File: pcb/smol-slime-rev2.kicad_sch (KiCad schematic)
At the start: 23 parts, among them J1 BATTERY, SW1 TS-1088-AR02016, U1 nPM1300, U2 LSM6DSV16X, U3 QMC6309

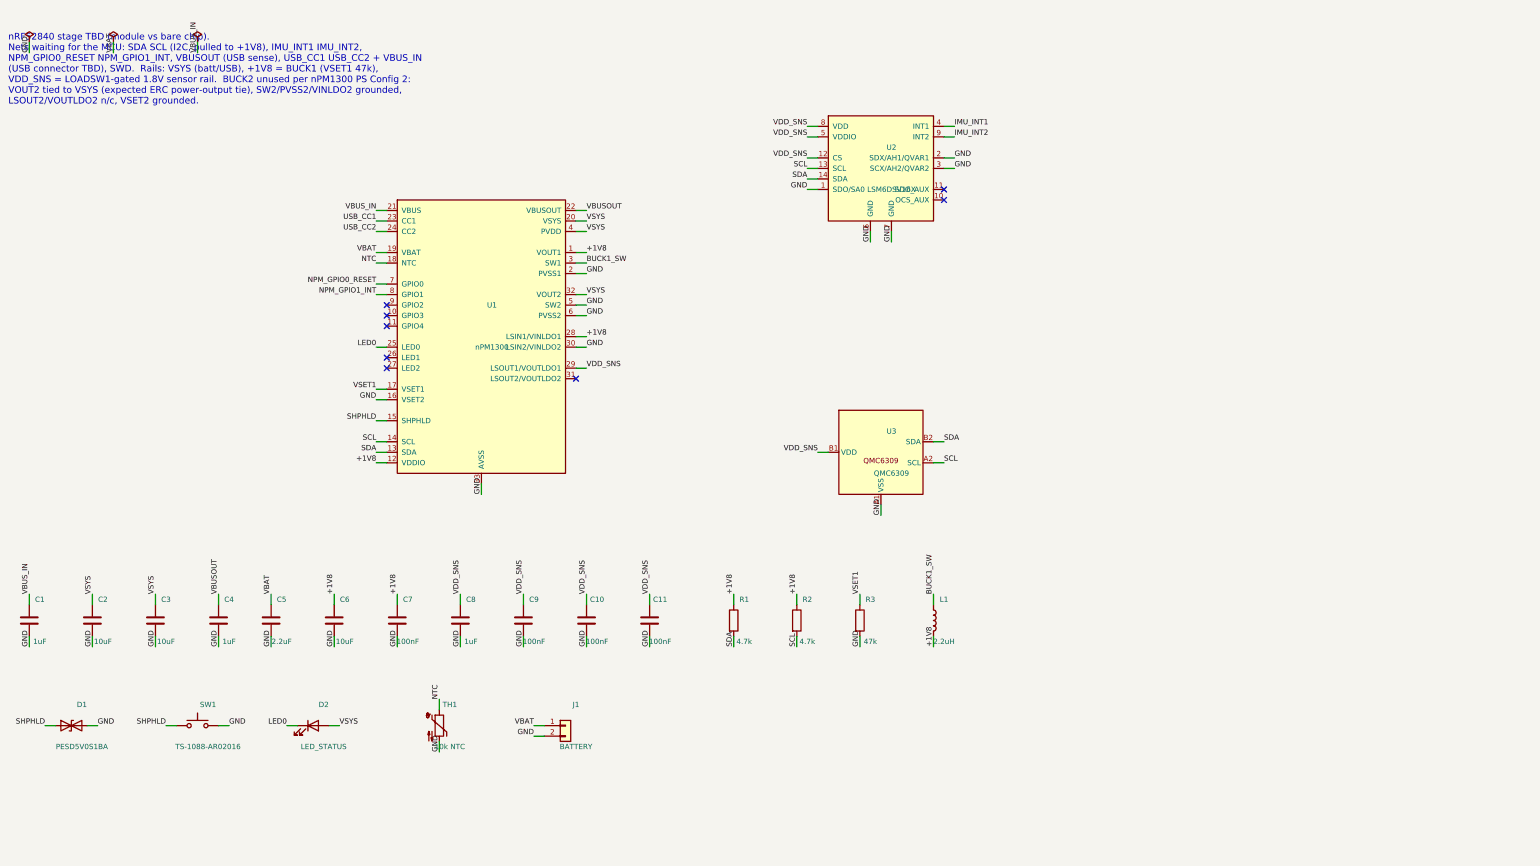
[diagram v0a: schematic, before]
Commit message: Wire the nRF52840 stage as a bare chip with custom antenna feed
The module route died on a supply reality: no JLCPCB-stocked nRF52840
module exposes its RF path for a custom on-PCB antenna. The Ebyte
E73-S1C keeps its ceramic antenna on the module, the S1CX only offers
an IPEX connector, and nothing from Raytac, Minew, or Holyiot is
stocked at all. The bare nRF52840-QIAA is meanwhile a Basic part with
over a thousand units, so rev 2 uses the bare chip and owns the
antenna.

The schematic now follows the nRF52840 Product Spec v1.11 section
7.3.5 circuit configuration 5: VDD and VDDH on the 1.8 V rail from the
nPM1300, REG1 DC/DC with the 15 nH plus 10 uH filter chain, the full
DEC decoupling set, a 32 MHz crystal with 12 pF loads, USB data lines
to labels pending a connector, and the reference RF match feeding an
RF_ANT net for the printed antenna. SWD and VTref/reset programming
pads use the existing PinPads footprints. The 32.768 kHz crystal is
omitted in favour of the LFRC, and NFC is unused. ERC findings are
down to the expected set enumerated in the sheet note.
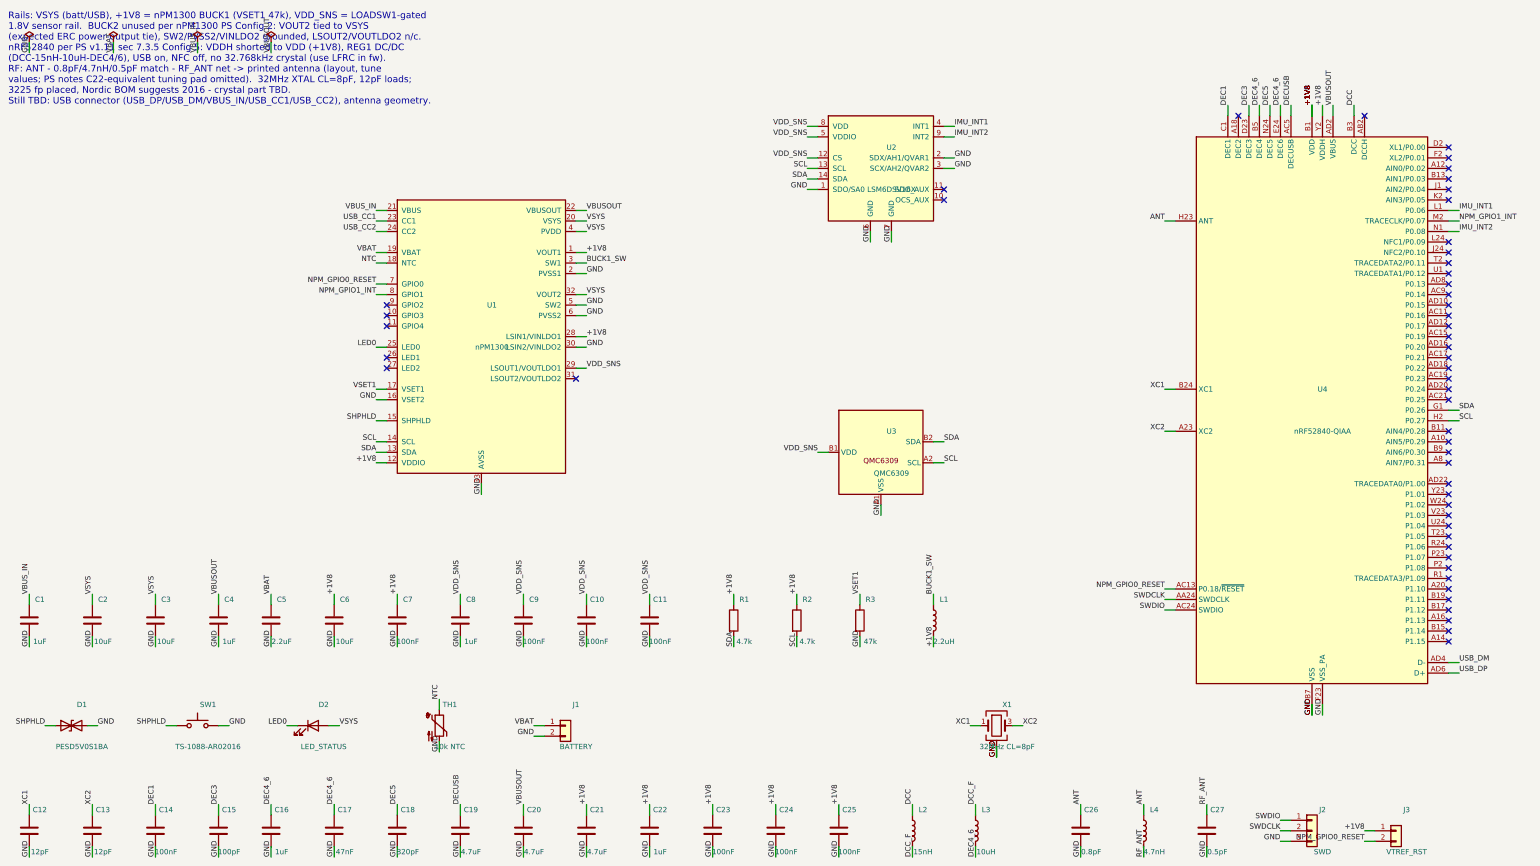
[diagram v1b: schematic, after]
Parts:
- added C12, C13: 12pF, Capacitor_SMD:C_0603_1608Metric, symbol Device:C
- added C14, C23, C24, C25: 100nF, Capacitor_SMD:C_0603_1608Metric, symbol Device:C
- added C15: 100pF, Capacitor_SMD:C_0603_1608Metric, symbol Device:C
- added C16, C22: 1uF, Capacitor_SMD:C_0603_1608Metric, symbol Device:C
- added C17: 47nF, Capacitor_SMD:C_0603_1608Metric, symbol Device:C
- added C18: 820pF, Capacitor_SMD:C_0603_1608Metric, symbol Device:C
- added C19, C20, C21: 4.7uF, Capacitor_SMD:C_0603_1608Metric, symbol Device:C
- added C26: 0.8pF, Capacitor_SMD:C_0402_1005Metric, symbol Device:C
- added C27: 0.5pF, Capacitor_SMD:C_0402_1005Metric, symbol Device:C
- added J2: SWD, smol-biscuits:PinPads_1x03_P2.54mm, symbol Connector_Generic:Conn_01x03
- added J3: VTREF_RST, smol-biscuits:PinPads_1x02_P2.54mm, symbol Connector_Generic:Conn_01x02
- added L2: 15nH, Inductor_SMD:L_0402_1005Metric, symbol Device:L
- added L3: 10uH, Inductor_SMD:L_0603_1608Metric, symbol Device:L
- added L4: 4.7nH, Inductor_SMD:L_0402_1005Metric, symbol Device:L
- added U4: nRF52840-QIAA, Package_DFN_QFN:Nordic_AQFN-73-1EP_7x7mm_P0.5mm, symbol MCU_Nordic:nRF52840
- added X1: 32MHz CL=8pF, smol-biscuits:Crystal_SMD_3225-4Pin_3.2x2.5mm_Silkscreenfix, symbol Device:Crystal_GND24
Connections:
- net +1V8: now also C21.1, C22.1, C23.1, C24.1, C25.1, J3.1 (Pin_1), U4.A22 (VDD), U4.AD14 (VDD), U4.AD23 (VDD), U4.B1 (VDD), U4.W1 (VDD), U4.Y2 (VDDH)
- net GND: now also C12.2, C13.2, C14.2, C15.2, C16.2, C17.2, C18.2, C19.2, C20.2, C21.2, C22.2, C23.2, C24.2, C25.2, C26.2, C27.2, J2.3 (Pin_3), U4.B7 (VSS), U4.EP (VSS), U4.F23 (VSS_PA), X1.2 (G), X1.4 (G)
- net IMU_INT1: now also U4.L1 (P0.06)
- net IMU_INT2: now also U4.N1 (P0.08)
- net NPM_GPIO0_RESET: now also J3.2 (Pin_2), U4.AC13 (P0.18/~{RESET})
- net NPM_GPIO1_INT: now also U4.M2 (TRACECLK/P0.07)
- net SCL: now also U4.H2 (P0.27)
- net SDA: now also U4.G1 (P0.26)
- net VBUSOUT: now also C20.1, U4.AD2 (VBUS)
- new net ANT: C26.1, L4.1, U4.H23 (ANT)
- new net DCC: L2.1, U4.B3 (DCC)
- new net DCC_F: L2.2, L3.1
- new net DEC1: C14.1, U4.C1 (DEC1)
- new net DEC3: C15.1, U4.D23 (DEC3)
- new net DEC4_6: C16.1, C17.1, L3.2, U4.B5 (DEC4), U4.E24 (DEC6)
- new net DEC5: C18.1, U4.N24 (DEC5)
- new net DECUSB: C19.1, U4.AC5 (DECUSB)
- new net RF_ANT: C27.1, L4.2
- new net SWDCLK: J2.2 (Pin_2), U4.AA24 (SWDCLK)
- new net SWDIO: J2.1 (Pin_1), U4.AC24 (SWDIO)
- new net USB_DM: U4.AD4 (D-)
- new net USB_DP: U4.AD6 (D+)
- new net XC1: C12.1, U4.B24 (XC1), X1.1
- new net XC2: C13.1, U4.A23 (XC2), X1.3
- no-connect marks 8 -> 52
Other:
- note added: "Rails: VSYS (batt/USB), +1V8 = nPM1300 BUCK1 (VSET1 47k), VDD_SNS = LOADSW1-gated 1.8V sensor rail. BUCK2 unused per nPM1300 PS Config 2: VOUT2 tied to VSYS (expected ERC power-output tie), SW2/PVSS2/VINLDO2 grounded, LSOUT2/VOUTLDO2 n/c. nRF52840 per PS v1.11 sec 7.3.5 Config 5: VDDH shorted to VDD (+1V8), REG1 DC/DC (DCC-15nH-10uH-DEC4/6), USB on, NFC off, no 32.768kHz crystal (use LFRC in fw).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"
- note removed: "nRF52840 stage TBD (module vs bare chip). Nets waiting for the MCU: SDA SCL (I2C, pulled to +1V8), IMU_INT1 IMU_INT2, NPM_GPIO0_RESET NPM_GPIO1_INT, VBUSOUT (USB sense), USB_CC1 USB_CC2 + VBUS_IN (USB connector TBD), SWD. Rails: VSYS (batt/USB), +1V8 = BUCK1 (VSET1 47k), VDD_SNS = LOADSW1-gated 1.8V sensor rail. BUCK2 unused per nPM1300 PS Config 2: VOUT2 tied to VSYS (expected ERC power-output t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"

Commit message: Add antenna tuning pad, part datasheets, and rev 2 handoff notes
The antenna is fully custom etched copper, so the schematic now carries
a DNP 0402 shunt pad at the RF_ANT feed for match tuning, mirroring the
N.C. provision in Nordic's reference circuit. Purchasing is no longer
assumed to go through JLCPCB assembly; parts may come from Digikey or
Mouser and be hand-soldered, which puts genuine manufacturers back on
the table for the TVS and friends.

docs/ gains the full datasheets for every rev 2 part: nRF52840 PS
v1.11, nPM1300 PS v1.1, LSM6DSV16X DS13510, the TS-1088 switch, and
the PESD5V0S1BA TVS. rev2-todo.md writes up the remaining work on
Sandra's side: antenna design and tuning, symbol and footprint reviews,
a distributor-friendly shopping list, the USB connector decision,
layout and hand-assembly notes, and the firmware task list.
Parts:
- added C28: DNP, Capacitor_SMD:C_0402_1005Metric, symbol Device:C
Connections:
- net GND: now also C28.2
- net RF_ANT: now also C28.1

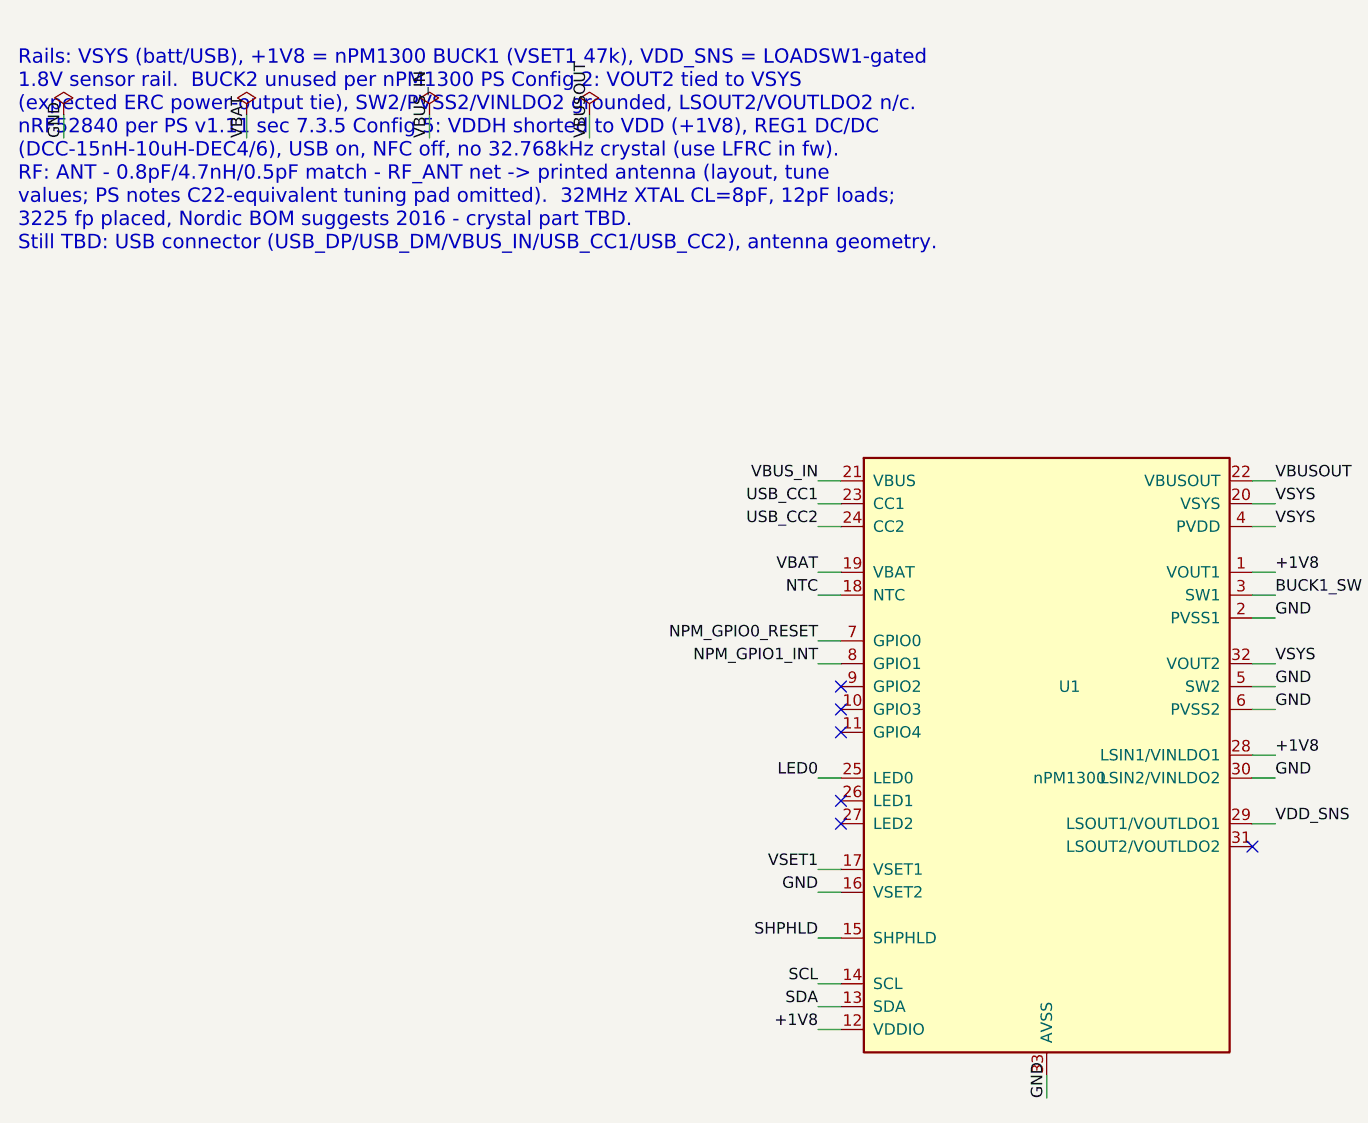
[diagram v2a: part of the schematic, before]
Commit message: Wire mid-mount USB-C connector
J4 is the Korean Hroparts TYPE-C-31-M-17, a mid-mount sink-type 16-pin
USB 2.0 receptacle at about nine cents, picked for the low-profile
wearable stack: the board gets a cutout and the connector hangs in it,
roughly halving the height. KiCad ships the footprint including the
cutout outline. VBUS, D+/D-, and the CC lines all land on the nPM1300
side nets; CC detection is inside the PMIC so the board carries no CC
resistors, SBU is no-connect, and the shell is grounded.

With the connector in, ERC is down to the four deliberate straps noted
on the sheet: the Nordic VOUT2 to VSYS tie, the VBUSOUT power flag,
and the IMU address and aux-disable grounds. The schematic has no
undriven or dangling nets left. Datasheet added to docs.
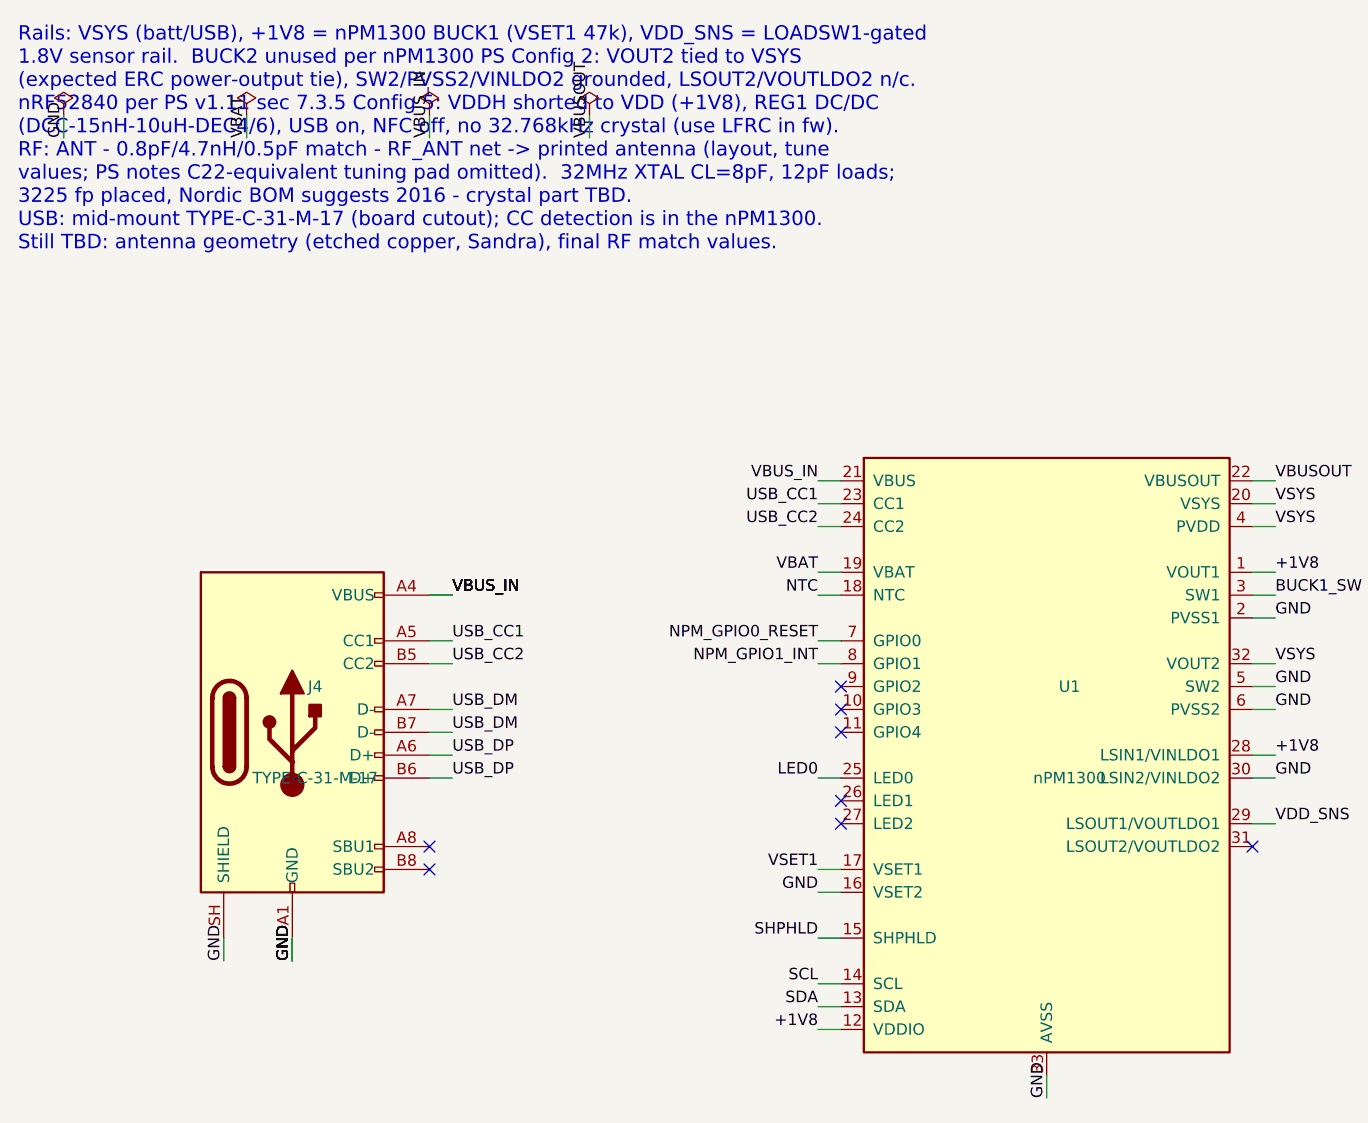
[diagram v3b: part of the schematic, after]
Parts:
- added J4: TYPE-C-31-M-17, Connector_USB:USB_C_Receptacle_HRO_TYPE-C-31-M-17, symbol Connector:USB_C_Receptacle_USB2.0_16P
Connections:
- net GND: now also J4.A1 (GND), J4.A12 (GND), J4.B1 (GND), J4.B12 (GND), J4.SH (SHIELD)
- net USB_CC1: now also J4.A5 (CC1)
- net USB_CC2: now also J4.B5 (CC2)
- net USB_DM: now also J4.A7 (D-), J4.B7 (D-)
- net USB_DP: now also J4.A6 (D+), J4.B6 (D+)
- net VBUS_IN: now also J4.A4 (VBUS), J4.A9 (VBUS), J4.B4 (VBUS), J4.B9 (VBUS)
- no-connect marks 52 -> 54

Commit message: Redraw rev 2 schematic with wired clusters and grouped placement
The first draft was pure stub-and-label netlist style, which is
electrically complete but reads as scattered parts. The sheet now draws
real wires for the circuits where shape carries meaning: the SHPHLD
button rail with the switch and TVS hanging in parallel, the BUCK1
switch node through the 2.2 uH inductor, and the RF chain from the ANT
ball through the 0.8 pF / 4.7 nH / 0.5 pF match and DNP tuning pad to
the RF_ANT feed. Decoupling and power distribution stay label-based as
usual, but every group now sits with its owner: crystal and load caps
by the XC pins, DEC caps under the nRF, sensor-rail caps by the IMU,
and the SWD pads beside the MCU. IC reference and value text moved
outside the symbol bodies.

Nothing electrical changed: the exported netlist is identical to the
previous commit across all 35 nets, and ERC still reports exactly the
four deliberate straps.
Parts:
- C12, C13: footprint Capacitor_SMD:C_0603_1608Metric -> Capacitor_SMD:C_0402_1005Metric

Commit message: Size passives per the Nordic reference BOMs
0603 everywhere was a hand-solder-friendly simplification inherited
from rev 1. The reference designs are one size finer for the small
values, and on a wearable the area matters, so the schematic now
matches them: sub-microfarad capacitors (100nF, 820pF, 100pF, 47nF,
12pF) and the three resistors move to 0402, joining the RF parts that
were already there. Bulk capacitors of a microfarad and up stay 0603
for DC-bias derating, and the NTC stays 0603 to suit the common 10k
thermistor parts. Net result: 21 passives at 0402, 15 at 0603.

Netlist verified identical; ERC unchanged.
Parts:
- C10, C11, C14, C15, C17, C18, C23, C24, C25, C7, C9: footprint Capacitor_SMD:C_0603_1608Metric -> Capacitor_SMD:C_0402_1005Metric
- R1, R2, R3: footprint Resistor_SMD:R_0603_1608Metric -> Resistor_SMD:R_0402_1005Metric
